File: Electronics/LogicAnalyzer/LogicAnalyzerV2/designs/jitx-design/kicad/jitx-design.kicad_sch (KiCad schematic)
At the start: 26 parts, among them J1 PM254-1-03-W-8.5, J2 C97095, J3 DZ254W-11-03-65, U1 TXU0104PWR, U2 TXU0104PWR, U3 TXU0104PWR, U4 TXU0104PWR, U5 TXU0104PWR, U6 TXU0104PWR, U7 PICO

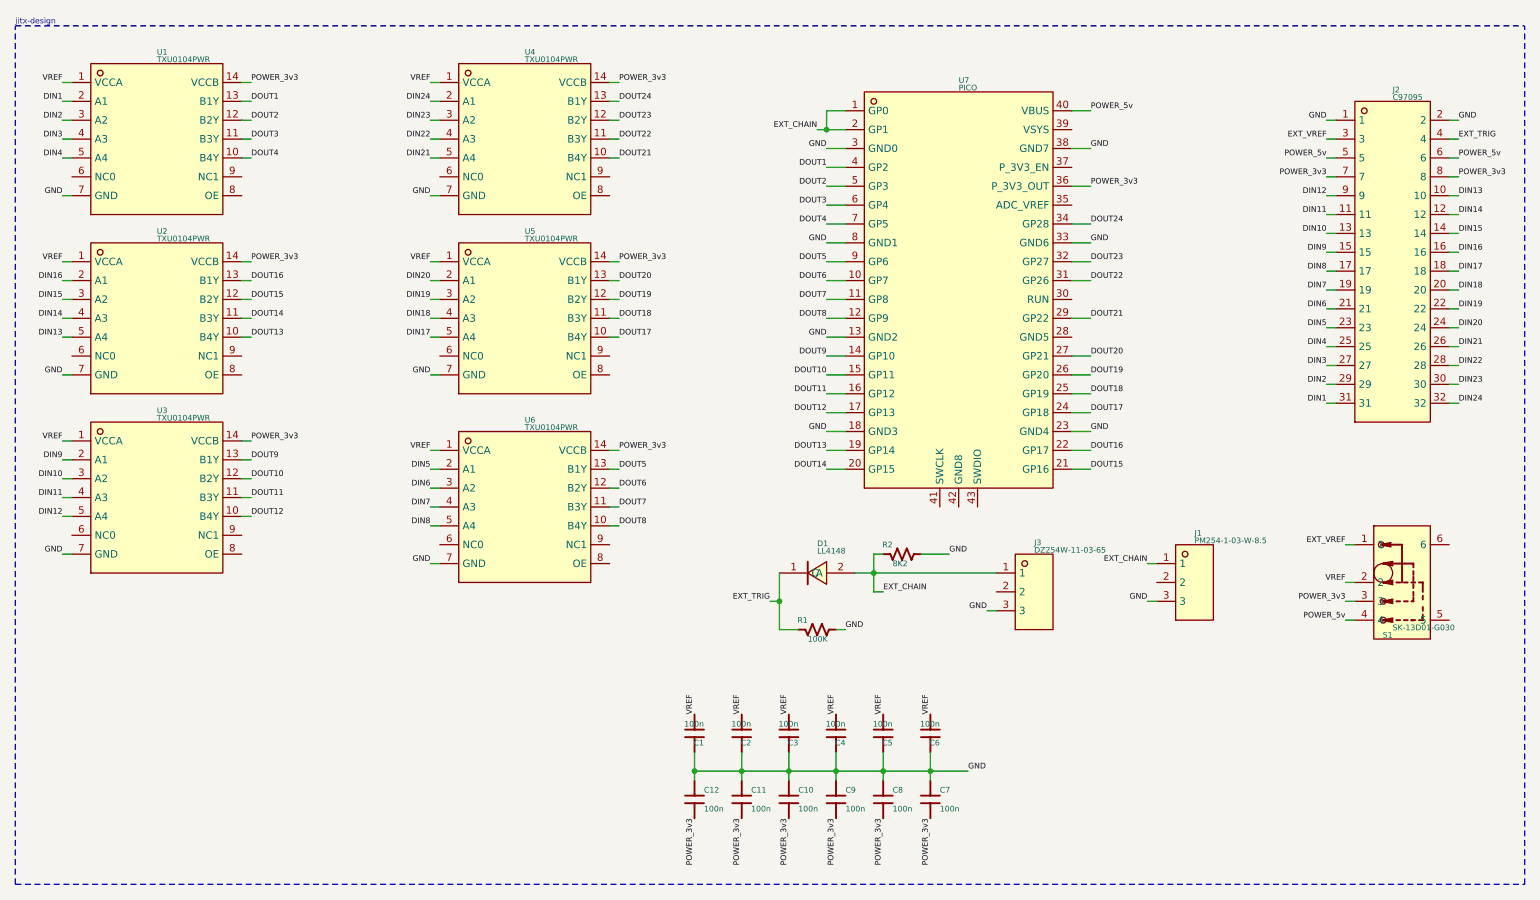
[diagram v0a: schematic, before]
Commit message: Pico 2 working with new PCB design
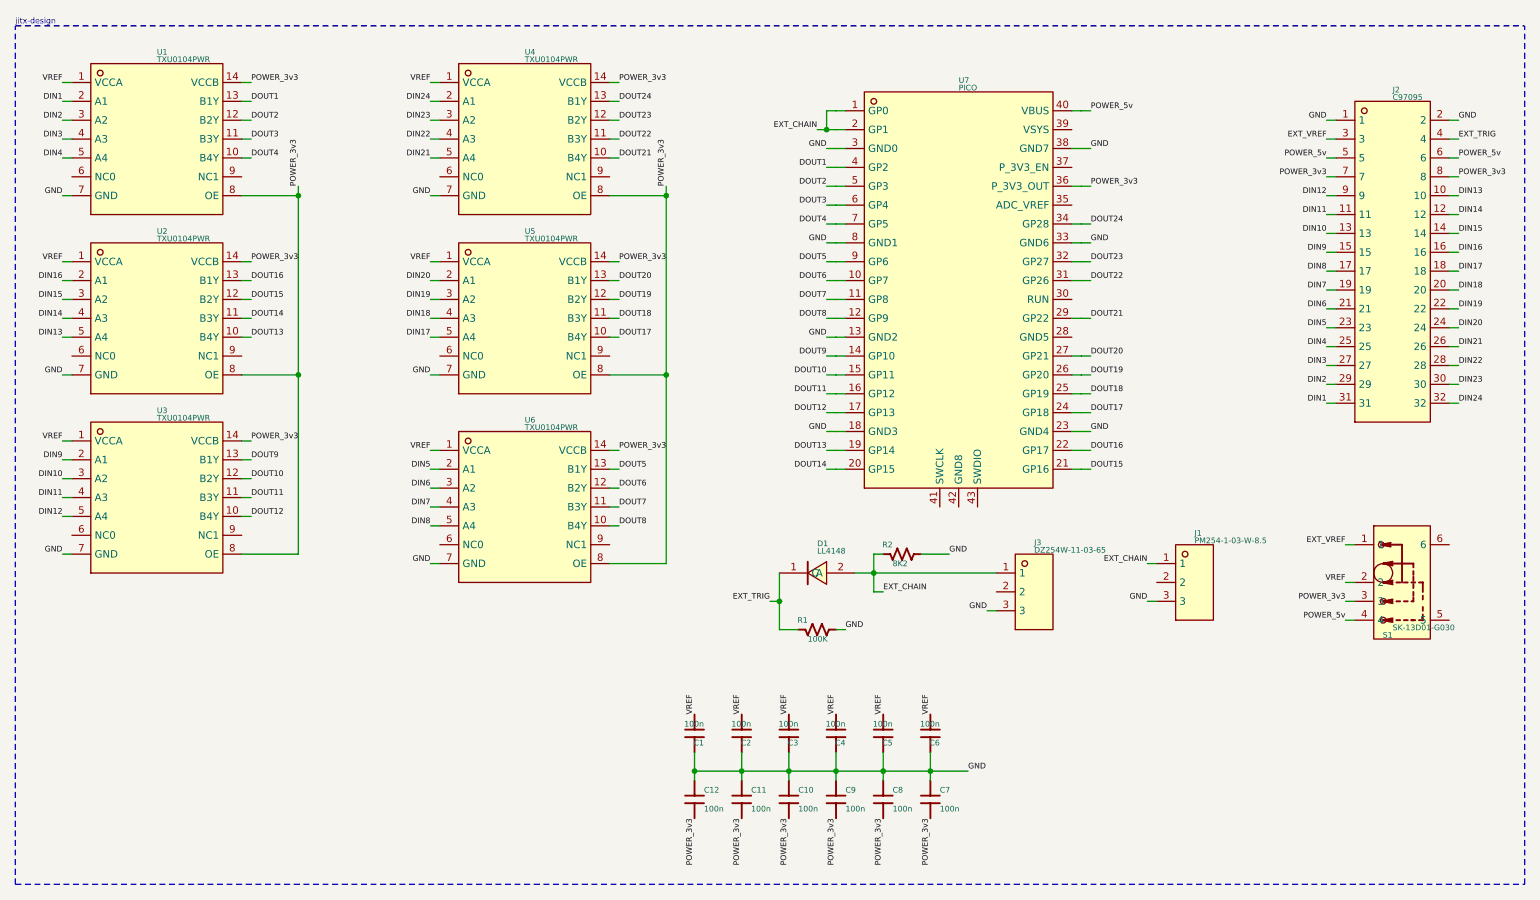
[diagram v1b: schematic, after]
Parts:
- removed C1: 100n, jitx-design:Pkg0402_6, symbol my_capacitor_4
- removed C10: 100n, jitx-design:Pkg0402, symbol my_capacitor_11
- removed C11: 100n, jitx-design:Pkg0402_4, symbol my_capacitor_3
- removed C12: 100n, jitx-design:Pkg0402_2, symbol my_capacitor_1
- removed C2: 100n, jitx-design:Pkg0402_3, symbol my_capacitor_2
- removed C3: 100n, jitx-design:Pkg0402_1, symbol my_capacitor
- removed C4: 100n, jitx-design:Pkg0402_8, symbol my_capacitor_6
- removed C5: 100n, jitx-design:Pkg0402_10, symbol my_capacitor_7
- removed C6: 100n, jitx-design:Pkg0402_12, symbol my_capacitor_9
- removed C7: 100n, jitx-design:Pkg0402_7, symbol my_capacitor_5
- removed C8: 100n, jitx-design:Pkg0402_11, symbol my_capacitor_8
- removed C9: 100n, jitx-design:Pkg0402_13, symbol my_capacitor_10
- removed R1: 100K, jitx-design:Pkg0402_9, symbol my_resistor_1
- removed R2: 8K2, jitx-design:Pkg0402_5, symbol my_resistor
- removed U1: TXU0104PWR, jitx-design:TSSOP_14_L5_0_W4_4_P0_65_LS6_4_BL_1, symbol C2938871_1
- removed U2: TXU0104PWR, jitx-design:TSSOP_14_L5_0_W4_4_P0_65_LS6_4_BL, symbol C2938871
- removed U3: TXU0104PWR, jitx-design:TSSOP_14_L5_0_W4_4_P0_65_LS6_4_BL_2, symbol C2938871_2
- removed U4: TXU0104PWR, jitx-design:TSSOP_14_L5_0_W4_4_P0_65_LS6_4_BL_5, symbol C2938871_5
- removed U5: TXU0104PWR, jitx-design:TSSOP_14_L5_0_W4_4_P0_65_LS6_4_BL_3, symbol C2938871_3
- removed U6: TXU0104PWR, jitx-design:TSSOP_14_L5_0_W4_4_P0_65_LS6_4_BL_4, symbol C2938871_4
- added C1: 100n, jitx-design:Pkg0402_13, symbol my_capacitor_11
- added C10: 100n, jitx-design:Pkg0402_7, symbol my_capacitor_6
- added C11: 100n, jitx-design:Pkg0402_11, symbol my_capacitor_10
- added C12: 100n, jitx-design:Pkg0402_9, symbol my_capacitor_8
- added C2: 100n, jitx-design:Pkg0402_10, symbol my_capacitor_9
- added C3: 100n, jitx-design:Pkg0402_8, symbol my_capacitor_7
- added C4: 100n, jitx-design:Pkg0402_2, symbol my_capacitor_1
- added C5: 100n, jitx-design:Pkg0402_3, symbol my_capacitor_2
- added C6: 100n, jitx-design:Pkg0402_5, symbol my_capacitor_4
- added C7: 100n, jitx-design:Pkg0402_1, symbol my_capacitor
- added C8: 100n, jitx-design:Pkg0402_4, symbol my_capacitor_3
- added C9: 100n, jitx-design:Pkg0402_6, symbol my_capacitor_5
- added R1: 100K, jitx-design:Pkg0402, symbol my_resistor
- added R2: 8K2, jitx-design:Pkg0402_12, symbol my_resistor_1
- added U1: TXU0104PWR, jitx-design:TSSOP_14_L5_0_W4_4_P0_65_LS6_4_BL_3, symbol C2938871_3
- added U2: TXU0104PWR, jitx-design:TSSOP_14_L5_0_W4_4_P0_65_LS6_4_BL_2, symbol C2938871_2
- added U3: TXU0104PWR, jitx-design:TSSOP_14_L5_0_W4_4_P0_65_LS6_4_BL_4, symbol C2938871_4
- added U4: TXU0104PWR, jitx-design:TSSOP_14_L5_0_W4_4_P0_65_LS6_4_BL_1, symbol C2938871_1
- added U5: TXU0104PWR, jitx-design:TSSOP_14_L5_0_W4_4_P0_65_LS6_4_BL_5, symbol C2938871_5
- added U6: TXU0104PWR, jitx-design:TSSOP_14_L5_0_W4_4_P0_65_LS6_4_BL, symbol C2938871
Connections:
- net DIN1: now also U1.2 (A1)
- net DIN10: now also U3.3 (A2)
- net DIN11: now also U3.4 (A3)
- net DIN12: now also U3.5 (A4)
- net DIN13: now also U2.5 (A4)
- net DIN14: now also U2.4 (A3)
- net DIN15: now also U2.3 (A2)
- net DIN16: now also U2.2 (A1)
- net DIN17: now also U5.5 (A4)
- net DIN18: now also U5.4 (A3)
- net DIN19: now also U5.3 (A2)
- net DIN2: now also U1.3 (A2)
- net DIN20: now also U5.2 (A1)
- net DIN21: now also U4.5 (A4)
- net DIN22: now also U4.4 (A3)
- net DIN23: now also U4.3 (A2)
- net DIN24: now also U4.2 (A1)
- net DIN3: now also U1.4 (A3)
- net DIN4: now also U1.5 (A4)
- net DIN5: now also U6.2 (A1)
- net DIN6: now also U6.3 (A2)
- net DIN7: now also U6.4 (A3)
- net DIN8: now also U6.5 (A4)
- net DIN9: now also U3.2 (A1)
- net DOUT1: now also U1.13 (B1Y)
- net DOUT10: now also U3.12 (B2Y)
- net DOUT11: now also U3.11 (B3Y)
- net DOUT12: now also U3.10 (B4Y)
- net DOUT13: now also U2.10 (B4Y)
- net DOUT14: now also U2.11 (B3Y)
- net DOUT15: now also U2.12 (B2Y)
- net DOUT16: now also U2.13 (B1Y)
- net DOUT17: now also U5.10 (B4Y)
- net DOUT18: now also U5.11 (B3Y)
- net DOUT19: now also U5.12 (B2Y)
- net DOUT2: now also U1.12 (B2Y)
- net DOUT20: now also U5.13 (B1Y)
- net DOUT21: now also U4.10 (B4Y)
- net DOUT22: now also U4.11 (B3Y)
- net DOUT23: now also U4.12 (B2Y)
- net DOUT24: now also U4.13 (B1Y)
- net DOUT3: now also U1.11 (B3Y)
- net DOUT4: now also U1.10 (B4Y)
- net DOUT5: now also U6.13 (B1Y)
- net DOUT6: now also U6.12 (B2Y)
- net DOUT7: now also U6.11 (B3Y)
- net DOUT8: now also U6.10 (B4Y)
- net DOUT9: now also U3.13 (B1Y)
- net EXT_CHAIN: now also R2.1
- net EXT_TRIG: now also R1.1
- net GND: now also C1.1, C10.1, C11.1, C12.1, C2.1, C3.1, C4.1, C5.1, C6.1, C7.1, C8.1, C9.1, R1.2, R2.2, U1.7 (GND), U2.7 (GND), U3.7 (GND), U4.7 (GND), U5.7 (GND), U6.7 (GND)
- net POWER_3v3: now also C10.2, C11.2, C12.2, C7.2, C8.2, C9.2, U1.14 (VCCB), U1.8 (OE), U2.14 (VCCB), U2.8 (OE), U3.14 (VCCB), U3.8 (OE), U4.14 (VCCB), U4.8 (OE), U5.14 (VCCB), U5.8 (OE), U6.14 (VCCB), U6.8 (OE)
- net VREF: now also C1.2, C2.2, C3.2, C4.2, C5.2, C6.2, U1.1 (VCCA), U2.1 (VCCA), U3.1 (VCCA), U4.1 (VCCA), U5.1 (VCCA), U6.1 (VCCA)

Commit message: Updated gitignore
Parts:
- removed C1: 100n, jitx-design:Pkg0402_13, symbol my_capacitor_11
- removed C10: 100n, jitx-design:Pkg0402_7, symbol my_capacitor_6
- removed C11: 100n, jitx-design:Pkg0402_11, symbol my_capacitor_10
- removed C12: 100n, jitx-design:Pkg0402_9, symbol my_capacitor_8
- removed C2: 100n, jitx-design:Pkg0402_10, symbol my_capacitor_9
- removed C3: 100n, jitx-design:Pkg0402_8, symbol my_capacitor_7
- removed C4: 100n, jitx-design:Pkg0402_2, symbol my_capacitor_1
- removed C5: 100n, jitx-design:Pkg0402_3, symbol my_capacitor_2
- removed C6: 100n, jitx-design:Pkg0402_5, symbol my_capacitor_4
- removed C7: 100n, jitx-design:Pkg0402_1, symbol my_capacitor
- removed C8: 100n, jitx-design:Pkg0402_4, symbol my_capacitor_3
- removed C9: 100n, jitx-design:Pkg0402_6, symbol my_capacitor_5
- removed R1: 100K, jitx-design:Pkg0402, symbol my_resistor
- removed R2: 8K2, jitx-design:Pkg0402_12, symbol my_resistor_1
- removed U1: TXU0104PWR, jitx-design:TSSOP_14_L5_0_W4_4_P0_65_LS6_4_BL_3, symbol C2938871_3
- removed U2: TXU0104PWR, jitx-design:TSSOP_14_L5_0_W4_4_P0_65_LS6_4_BL_2, symbol C2938871_2
- removed U3: TXU0104PWR, jitx-design:TSSOP_14_L5_0_W4_4_P0_65_LS6_4_BL_4, symbol C2938871_4
- removed U4: TXU0104PWR, jitx-design:TSSOP_14_L5_0_W4_4_P0_65_LS6_4_BL_1, symbol C2938871_1
- removed U5: TXU0104PWR, jitx-design:TSSOP_14_L5_0_W4_4_P0_65_LS6_4_BL_5, symbol C2938871_5
- removed U6: TXU0104PWR, jitx-design:TSSOP_14_L5_0_W4_4_P0_65_LS6_4_BL, symbol C2938871
- added C1: 100n, jitx-design:Pkg0402_3, symbol my_capacitor_2
- added C10: 100n, jitx-design:Pkg0402_11, symbol my_capacitor_9
- added C11: 100n, jitx-design:Pkg0402_1, symbol my_capacitor_1
- added C12: 100n, jitx-design:Pkg0402_13, symbol my_capacitor_11
- added C2: 100n, jitx-design:Pkg0402, symbol my_capacitor
- added C3: 100n, jitx-design:Pkg0402_12, symbol my_capacitor_10
- added C4: 100n, jitx-design:Pkg0402_6, symbol my_capacitor_4
- added C5: 100n, jitx-design:Pkg0402_7, symbol my_capacitor_5
- added C6: 100n, jitx-design:Pkg0402_9, symbol my_capacitor_7
- added C7: 100n, jitx-design:Pkg0402_5, symbol my_capacitor_3
- added C8: 100n, jitx-design:Pkg0402_8, symbol my_capacitor_6
- added C9: 100n, jitx-design:Pkg0402_10, symbol my_capacitor_8
- added R1: 100K, jitx-design:Pkg0402_4, symbol my_resistor_1
- added R2: 8K2, jitx-design:Pkg0402_2, symbol my_resistor
- added U1: TXU0104PWR, jitx-design:TSSOP_14_L5_0_W4_4_P0_65_LS6_4_BL_5, symbol C2938871_5
- added U2: TXU0104PWR, jitx-design:TSSOP_14_L5_0_W4_4_P0_65_LS6_4_BL_4, symbol C2938871_4
- added U3: TXU0104PWR, jitx-design:TSSOP_14_L5_0_W4_4_P0_65_LS6_4_BL, symbol C2938871
- added U4: TXU0104PWR, jitx-design:TSSOP_14_L5_0_W4_4_P0_65_LS6_4_BL_3, symbol C2938871_3
- added U5: TXU0104PWR, jitx-design:TSSOP_14_L5_0_W4_4_P0_65_LS6_4_BL_1, symbol C2938871_1
- added U6: TXU0104PWR, jitx-design:TSSOP_14_L5_0_W4_4_P0_65_LS6_4_BL_2, symbol C2938871_2
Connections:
- net DIN1: now also U1.2 (A1)
- net DIN10: now also U3.3 (A2)
- net DIN11: now also U3.4 (A3)
- net DIN12: now also U3.5 (A4)
- net DIN13: now also U2.5 (A4)
- net DIN14: now also U2.4 (A3)
- net DIN15: now also U2.3 (A2)
- net DIN16: now also U2.2 (A1)
- net DIN17: now also U5.5 (A4)
- net DIN18: now also U5.4 (A3)
- net DIN19: now also U5.3 (A2)
- net DIN2: now also U1.3 (A2)
- net DIN20: now also U5.2 (A1)
- net DIN21: now also U4.5 (A4)
- net DIN22: now also U4.4 (A3)
- net DIN23: now also U4.3 (A2)
- net DIN24: now also U4.2 (A1)
- net DIN3: now also U1.4 (A3)
- net DIN4: now also U1.5 (A4)
- net DIN5: now also U6.2 (A1)
- net DIN6: now also U6.3 (A2)
- net DIN7: now also U6.4 (A3)
- net DIN8: now also U6.5 (A4)
- net DIN9: now also U3.2 (A1)
- net DOUT1: now also U1.13 (B1Y)
- net DOUT10: now also U3.12 (B2Y)
- net DOUT11: now also U3.11 (B3Y)
- net DOUT12: now also U3.10 (B4Y)
- net DOUT13: now also U2.10 (B4Y)
- net DOUT14: now also U2.11 (B3Y)
- net DOUT15: now also U2.12 (B2Y)
- net DOUT16: now also U2.13 (B1Y)
- net DOUT17: now also U5.10 (B4Y)
- net DOUT18: now also U5.11 (B3Y)
- net DOUT19: now also U5.12 (B2Y)
- net DOUT2: now also U1.12 (B2Y)
- net DOUT20: now also U5.13 (B1Y)
- net DOUT21: now also U4.10 (B4Y)
- net DOUT22: now also U4.11 (B3Y)
- net DOUT23: now also U4.12 (B2Y)
- net DOUT24: now also U4.13 (B1Y)
- net DOUT3: now also U1.11 (B3Y)
- net DOUT4: now also U1.10 (B4Y)
- net DOUT5: now also U6.13 (B1Y)
- net DOUT6: now also U6.12 (B2Y)
- net DOUT7: now also U6.11 (B3Y)
- net DOUT8: now also U6.10 (B4Y)
- net DOUT9: now also U3.13 (B1Y)
- net EXT_CHAIN: now also R2.1
- net EXT_TRIG: now also R1.1
- net GND: now also C1.1, C10.1, C11.1, C12.1, C2.1, C3.1, C4.1, C5.1, C6.1, C7.1, C8.1, C9.1, R1.2, R2.2, U1.7 (GND), U2.7 (GND), U3.7 (GND), U4.7 (GND), U5.7 (GND), U6.7 (GND)
- net POWER_3v3: now also C10.2, C11.2, C12.2, C7.2, C8.2, C9.2, U1.14 (VCCB), U1.8 (OE), U2.14 (VCCB), U2.8 (OE), U3.14 (VCCB), U3.8 (OE), U4.14 (VCCB), U4.8 (OE), U5.14 (VCCB), U5.8 (OE), U6.14 (VCCB), U6.8 (OE)
- net VREF: now also C1.2, C2.2, C3.2, C4.2, C5.2, C6.2, U1.1 (VCCA), U2.1 (VCCA), U3.1 (VCCA), U4.1 (VCCA), U5.1 (VCCA), U6.1 (VCCA)
